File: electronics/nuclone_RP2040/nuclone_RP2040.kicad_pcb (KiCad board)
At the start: 4 copper layers, 50 x 50 mm, 42 parts, among them J1 JTAG_2X05, J2 TYPE-C-31-M-12, J3 nuclone_small_left, J4 nuclone_small_right, SW1 RESET, SW2 Bootloader, U1 MCP1702-MB, U2 TPESD0504C6

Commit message: WIP placing
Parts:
- added C10: 1u, SquantorRcl:C_0402, F.Cu at (90.3, 87.8)
- added C11: 22p, SquantorRcl:C_0402, F.Cu at (91.0, 102.4)
- added C12: 22p, SquantorRcl:C_0402, F.Cu at (93.6, 102.9)
- added C13: 1u, SquantorRcl:C_0402, F.Cu at (90.3, 91.4)
- added C15: 1u, SquantorRcl:C_0402, F.Cu at (86.4, 95.7)
- added C16: 1u, SquantorRcl:C_0402, F.Cu at (85.0, 84.6)
- added C18: 1u, SquantorRcl:C_0402, F.Cu at (87.2, 84.6)
- added C19: 1u, SquantorRcl:C_0402, F.Cu at (89.8, 86.1)
- added C20: 1u, SquantorRcl:C_0402, F.Cu at (88.3, 84.6)
- added C21: 1u, SquantorRcl:C_0402, F.Cu at (83.9, 84.6)
- added C5: 1u, SquantorRcl:C_0402, F.Cu at (79.7, 87.8)
- added C6: 1u, SquantorRcl:C_0402, F.Cu at (79.7, 91.4)
- added C7: 1u, SquantorRcl:C_0402, F.Cu at (85.3, 95.7)
- added C8: 1u, SquantorRcl:C_0402, F.Cu at (86.1, 84.6)
- added FB2: 600, SquantorRcl:L_0402, F.Cu at (90.9, 86.1)
- added R9: TBD, SquantorRcl:R_0402_hand, F.Cu at (84.2, 95.7)
- added U3: rp2040, SquantorIC:QFN56_7by7mm_RaspberryPi, F.Cu at (85.0, 90.4)
- added Y1: 12MHz, SquantorCrystal:Crystal_3225_4, F.Cu at (90.0, 98.7)
- N1: footprint Symbols:OSHW-Symbol_6.7x6mm_SilkScreen -> Symbol:OSHW-Symbol_6.7x6mm_SilkScreen
- N2: value V20220515 -> V20220527
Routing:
- net /VSS: vias 17 -> 16

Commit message: updated design rules, fixed some DRC errors
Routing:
- net /VSS: track 24.7 -> 24.3 mm, vias 16 -> 12
- net /TDO: vias 1 -> 0
- net /TDI: vias 1 -> 0

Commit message: added serial flash
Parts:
- added C22: 1u, SquantorRcl:C_0402, F.Cu at (86.7, 82.4)
- added C23: 10u, SquantorRcl:C_0603, F.Cu at (87.0, 80.1)
- added U4: MX25L3233FZBI, SquantorIC:USON-8-4x3-Macronix, F.Cu at (82.7, 81.8)
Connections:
- U3 pad 51: unconnected-(U3-Pad51) -> /microcontroller/QSPI_SD3
- U3 pad 52: unconnected-(U3-Pad52) -> /microcontroller/QSPI_SCLK
- U3 pad 53: unconnected-(U3-Pad53) -> /microcontroller/QSPI_SD0
- U3 pad 54: unconnected-(U3-Pad54) -> /microcontroller/QSPI_SD2
- U3 pad 55: unconnected-(U3-Pad55) -> /microcontroller/QSPI_SD1
- U3 pad 56: unconnected-(U3-Pad56) -> /microcontroller/QSPI_SS
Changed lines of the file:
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@@
   (net 57 "/microcontroller/AVDD")
   (net 58 "Net-(R9-Pad2)")
-  (net 59 "unconnected-(U3-Pad51)")
-  (net 60 "unconnected-(U3-Pad52)")
-  (net 61 "unconnected-(U3-Pad53)")
-  (net 62 "unconnected-(U3-Pad54)")
-  (net 63 "unconnected-(U3-Pad55)")
-  (net 64 "unconnected-(U3-Pad56)")
+  (net 59 "/microcontroller/QSPI_SD3")
+  (net 60 "/microcontroller/QSPI_SCLK")
+  (net 61 "/microcontroller/QSPI_SD0")
+  (net 62 "/microcontroller/QSPI_SD2")
+  (net 63 "/microcontroller/QSPI_SD1")
+  (net 64 "/microcontroller/QSPI_SS")
   (footprint "MountingHole:MountingHole_3.2mm_M3_Pad_Via" locked (layer "F.Cu")
     (at 63.7 64.7)
@@
   )
   (footprint "SquantorRcl:C_0402" (layer "F.Cu")
+    (at 86.7 82.4)
+    (descr "Capacitor SMD 0402, reflow soldering, AVX (see smccp.pdf)")
+    (tags "capacitor 0402")
+    (property "Sheetfile" "microcontroller.kicad_sch")
+    (property "Sheetname" "microcontroller")
+    (attr smd)
+    (fp_text reference "C22" (at 0 -1.7) (layer "F.SilkS")
+      (effects (font (size 1 1) (thickness 0.15)))
+    )
+    (fp_text value "1u" (at 0 1.7) (layer "F.Fab")
+      (effects (font (size 1 1) (thickness 0.15)))
+    )
+    (fp_line (start 0 -0.2) (end 0 0.2) (layer "F.SilkS") (width 0.15))
+    (fp_line (start 1.1 -0.55) (end 1.1 0.55) (layer "F.CrtYd") (width 0.05))
+    (fp_line (start -1.1 -0.55) (end 1.1 -0.55) (layer "F.CrtYd") (width 0.05))
+    (fp_line (start -1.1 -0.55) (end -1.1 0.55) (layer "F.CrtYd") (width 0.05))
+    (fp_line (start -1.1 0.55) (end 1.1 0.55) (layer "F.CrtYd") (width 0.05))
+    (fp_line (start 0.5 0.25) (end -0.5 0.25) (layer "F.Fab") (width 0.1))
+    (fp_line (start -0.5 0.25) (end -0.5 -0.25) (layer "F.Fab") (width 0.1))
+    (fp_line (start -0.5 -0.25) (end 0.5 -0.25) (layer "F.Fab") (width 0.1))
+    (fp_line (start 0.5 -0.25) (end 0.5 0.25) (layer "F.Fab") (width 0.1))
+    (pad "1" smd rect (at -0.55 0) (size 0.6 0.6) (layers "F.Cu" "F.Paste" "F.Mask")
+      (net 5 "/VSS") (pintype "passive"))
+    (pad "2" smd rect (at 0.55 0) (size 0.6 0.6) (layers "F.Cu" "F.Paste" "F.Mask")
+      (net 3 "/VDD") (pintype "passive"))
+    (model "${KICAD6_3DMODEL_DIR}//Capacitor_SMD.3dshapes/C_0402_1005Metric.step"
+      (offset (xyz 0 0 0))
+      (scale (xyz 1 1 1))
+      (rotate (xyz 0 0 0))
+    )
+  )
+  (footprint "SquantorRcl:C_0402" (layer "F.Cu")
     (at 86.4 95.7 90)
     (descr "Capacitor SMD 0402, reflow soldering, AVX (see smccp.pdf)")
@@
       (net 56 "/microcontroller/1.1V") (pinfunction "DVDD") (pintype "power_in"))
     (pad "51" smd rect (at -0.6 -3.4375 270) (size 0.875 0.2) (layers "F.Cu" "F.Paste" "F.Mask")
-      (net 59 "unconnected-(U3-Pad51)") (pinfunction "QSPI_SD3") (pintype "bidirectional"))
+      (net 59 "/microcontroller/QSPI_SD3") (pinfunction "QSPI_SD3") (pintype "bidirectional"))
     (pad "52" smd rect (at -1 -3.4375 270) (size 0.875 0.2) (layers "F.Cu" "F.Paste" "F.Mask")
-      (net 60 "unconnected-(U3-Pad52)") (pinfunction "QSPI_SCLK") (pintype "output"))
+      (net 60 "/microcontroller/QSPI_SCLK") (pinfunction "QSPI_SCLK") (pintype "output"))
     (pad "53" smd rect (at -1.4 -3.4375 270) (size 0.875 0.2) (layers "F.Cu" "F.Paste" "F.Mask")
-      (net 61 "unconnected-(U3-Pad53)") (pinfunction "QSPI_SD0") (pintype "bidirectional"))
+      (net 61 "/microcontroller/QSPI_SD0") (pinfunction "QSPI_SD0") (pintype "bidirectional"))
     (pad "54" smd rect (at -1.8 -3.4375 270) (size 0.875 0.2) (layers "F.Cu" "F.Paste" "F.Mask")
-      (net 62 "unconnected-(U3-Pad54)") (pinfunction "QSPI_SD2") (pintype "bidirectional"))
+      (net 62 "/microcontroller/QSPI_SD2") (pinfunction "QSPI_SD2") (pintype "bidirectional"))
     (pad "55" smd rect (at -2.2 -3.4375 270) (size 0.875 0.2) (layers "F.Cu" "F.Paste" "F.Mask")
-      (net 63 "unconnected-(U3-Pad55)") (pinfunction "QSPI_SD1") (pintype "bidirectional"))
+      (net 63 "/microcontroller/QSPI_SD1") (pinfunction "QSPI_SD1") (pintype "bidirectional"))
     (pad "56" smd rect (at -2.6 -3.4375 270) (size 0.875 0.2) (layers "F.Cu" "F.Paste" "F.Mask")
-      (net 64 "unconnected-(U3-Pad56)") (pinfunction "QSPI_SS_N") (pintype "output"))
+      (net 64 "/microcontroller/QSPI_SS") (pinfunction "QSPI_SS_N") (pintype "output"))
     (pad "57" smd rect (at 0 0) (size 3.2 3.2) (layers "F.Cu")
       (net 5 "/VSS") (pinfunction "GND") (pintype "power_in"))
@@
       (rotate (xyz 0 0 0))
     )
+  )
+  (footprint "SquantorRcl:C_0603" (layer "F.Cu")
+    (at 87 80.1)
+    (descr "Capacitor SMD 0603, reflow soldering, AVX (see smccp.pdf)")
+    (tags "capacitor 0603")
+    (property "Sheetfile" "microcontroller.kicad_sch")
+    (property "Sheetname" "microcontroller")
+    (attr smd)
+    (fp_text reference "C23" (at 0 -1.9) (layer "F.SilkS")
+      (effects (font (size 1 1) (thickness 0.15)))
+    )
+    (fp_text value "10u" (at 0 1.9) (layer "F.Fab")
+      (effects (font (size 1 1) (thickness 0.15)))
+    )
+    (fp_line (start 0 -0.35) (end 0 0.35) (layer "F.SilkS") (width 0.15))
+    (fp_line (start -1.4 0.7) (end 1.4 0.7) (layer "F.CrtYd") (width 0.05))
+    (fp_line (start 1.4 -0.7) (end 1.4 0.7) (layer "F.CrtYd") (width 0.05))
+    (fp_line (start -1.4 -0.7) (end -1.4 0.7) (layer "F.CrtYd") (width 0.05))
+    (fp_line (start -1.4 -0.7) (end 1.4 -0.7) (layer "F.CrtYd") (width 0.05))
+    (fp_line (start -0.8 -0.4) (end 0.8 -0.4) (layer "F.Fab") (width 0.1))
+    (fp_line (start 0.8 -0.4) (end 0.8 0.4) (layer "F.Fab") (width 0.1))
+    (fp_line (start -0.8 0.4) (end -0.8 -0.4) (layer "F.Fab") (width 0.1))
+    (fp_line (start 0.8 0.4) (end -0.8 0.4) (layer "F.Fab") (width 0.1))
+    (pad "1" smd rect (at -0.75 0) (size 0.8 0.9) (layers "F.Cu" "F.Paste" "F.Mask")
+      (net 5 "/VSS") (pintype "passive"))
+    (pad "2" smd rect (at 0.75 0) (size 0.8 0.9) (layers "F.Cu" "F.Paste" "F.Mask")
+      (net 3 "/VDD") (pintype "passive"))
+    (model "${KICAD6_3DMODEL_DIR}/Capacitor_SMD.3dshapes/C_0603_1608Metric.step"
+      (offset (xyz 0 0 0))
+      (scale (xyz 1 1 1))
+      (rotate (xyz 0 0 0))
+    )
+  )
+  (footprint "SquantorIC:USON-8-4x3-Macronix" (layer "F.Cu")
+    (at 82.665 81.835)
+    (descr "USON 8 pin 4 by 3mm size as specified by Macronix")
+    (tags "USON-8 4x3mm Macronix")
+    (property "Sheetfile" "microcontroller.kicad_sch")
+    (property "Sheetname" "microcontroller")
+    (attr smd)
+    (fp_text reference "U4" (at 0 -2.9) (layer "F.SilkS")
+      (effects (font (size 1 1) (thickness 0.15)))
+    )
+    (fp_text value "MX25L3233FZBI" (at 0 2.8) (layer "F.Fab")
+      (effects (font (size 1 1) (thickness 0.15)))
+    )
+    (fp_line (start -1.5 2) (end 1.5 2) (layer "F.SilkS") (width 0.12))
+    (fp_line (start 1.5 -2) (end -1.5 -2) (layer "F.SilkS") (width 0.12))
+    (fp_circle (center -1.7 -2.2) (end -1.5 -2.2) (layer "F.SilkS") (width 0.12) (fill none))
+    (fp_line (start -1.9 -2.3) (end -1.9 2.4) (layer "F.CrtYd") (width 0.025))
+    (fp_line (start 1.9 -2.3) (end -1.9 -2.3) (layer "F.CrtYd") (width 0.025))
+    (fp_line (start -1.9 2.4) (end 1.9 2.4) (layer "F.CrtYd") (width 0.025))
+    (fp_line (start 1.9 2.4) (end 1.9 -2.3) (layer "F.CrtYd") (width 0.025))
+    (fp_line (start -1.5 -2) (end -1.5 2) (layer "F.Fab") (width 0.1))
+    (fp_line (start 1.5 2) (end 1.5 -2) (layer "F.Fab") (width 0.1))
+    (pad "1" smd rect locked (at -1.2 -1.2) (size 0.8 0.4) (layers "F.Cu" "F.Paste" "F.Mask")
+      (net 64 "/microcontroller/QSPI_SS") (pinfunction "CS/") (pintype "input"))
+    (pad "2" smd rect locked (at -1.2 -0.4) (size 0.8 0.4) (layers "F.Cu" "F.Paste" "F.Mask")
+      (net 63 "/microcontroller/QSPI_SD1") (pinfunction "SO_SIO1") (pintype "bidirectional"))
+    (pad "3" smd rect locked (at -1.2 0.4) (size 0.8 0.4) (layers "F.Cu" "F.Paste" "F.Mask")
+      (net 62 "/microcontroller/QSPI_SD2") (pinfunction "WP/_SIO2") (pintype "bidirectional"))
+    (pad "4" smd rect locked (at -1.2 1.2) (size 0.8 0.4) (layers "F.Cu" "F.Paste" "F.Mask")
+      (net 5 "/VSS") (pinfunction "GND") (pintype "power_in"))
+    (pad "5" smd rect locked (at 1.2 1.2) (size 0.8 0.4) (layers "F.Cu" "F.Paste" "F.Mask")
+      (net 61 "/microcontroller/QSPI_SD0") (pinfunction "SI_SIO0") (pintype "power_in"))
+    (pad "6" smd rect locked (at 1.2 0.4) (size 0.8 0.4) (layers "F.Cu" "F.Paste" "F.Mask")
+      (net 60 "/microcontroller/QSPI_SCLK") (pinfunction "SCLK") (pintype "input"))
+    (pad "7" smd rect locked (at 1.2 -0.4) (size 0.8 0.4) (layers "F.Cu" "F.Paste" "F.Mask")
+      (net 59 "/microcontroller/QSPI_SD3") (pinfunction "HOLD/_SIO3") (pintype "bidirectional"))
+    (pad "8" smd rect locked (at 1.2 -1.2) (size 0.8 0.4) (layers "F.Cu" "F.Paste" "F.Mask")
+      (net 3 "/VDD") (pinfunction "VCC") (pintype "power_in"))
+    (pad "9" smd rect locked (at 0 -0.8) (size 0.2 0.8) (layers "F.Cu" "F.Paste" "F.Mask")
+      (net 5 "/VSS") (pinfunction "GND") (pintype "power_in"))
+    (pad "9" smd rect locked (at 0 0.8) (size 0.2 0.8) (layers "F.Cu" "F.Paste" "F.Mask")
+      (net 5 "/VSS") (pinfunction "GND") (pintype "power_in"))
+    (model "${KISYS3DMOD}/Package_SON.3dshapes/WSON-8_4x4mm_P0.8mm.step"
+      (offset (xyz 0 0 0))
+      (scale (xyz 0.7 1 1))
+      (rotate (xyz 0 0 0))
+    )

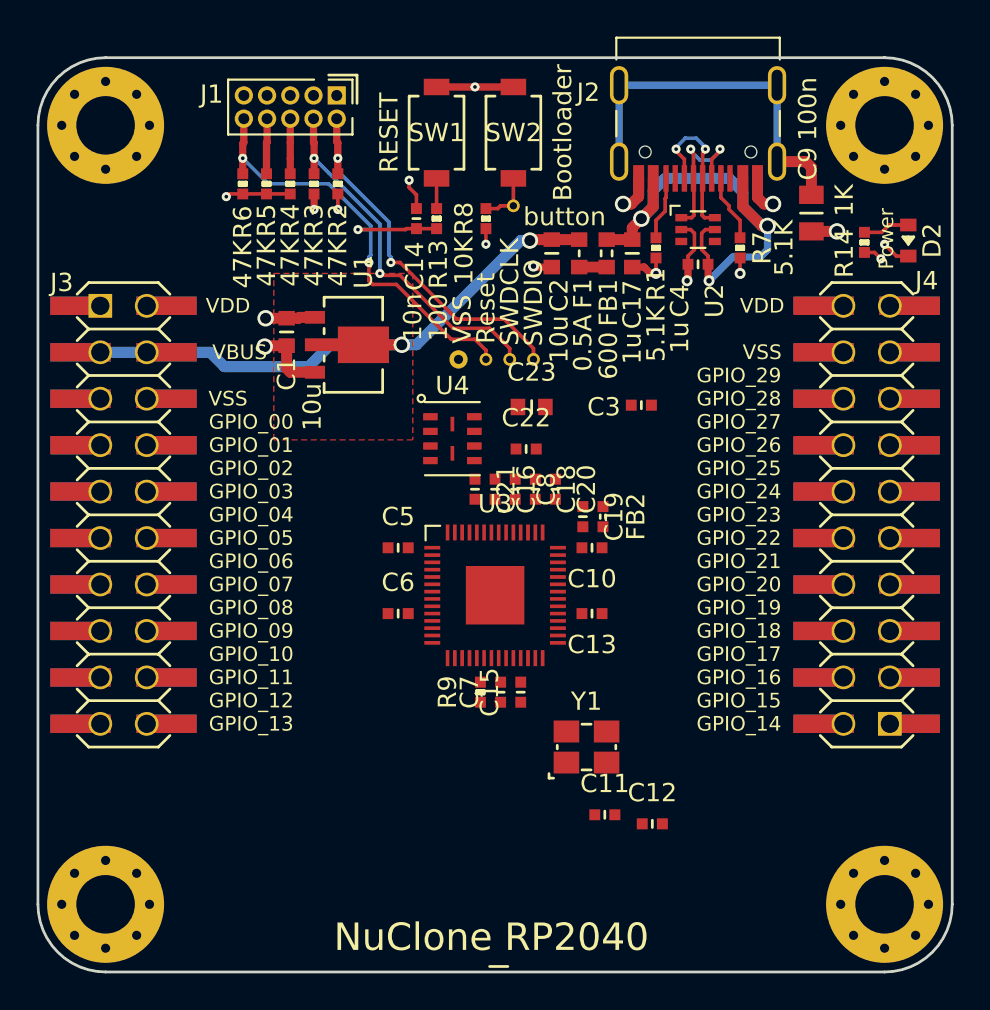
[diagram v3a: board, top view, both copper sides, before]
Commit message: further placing and routing
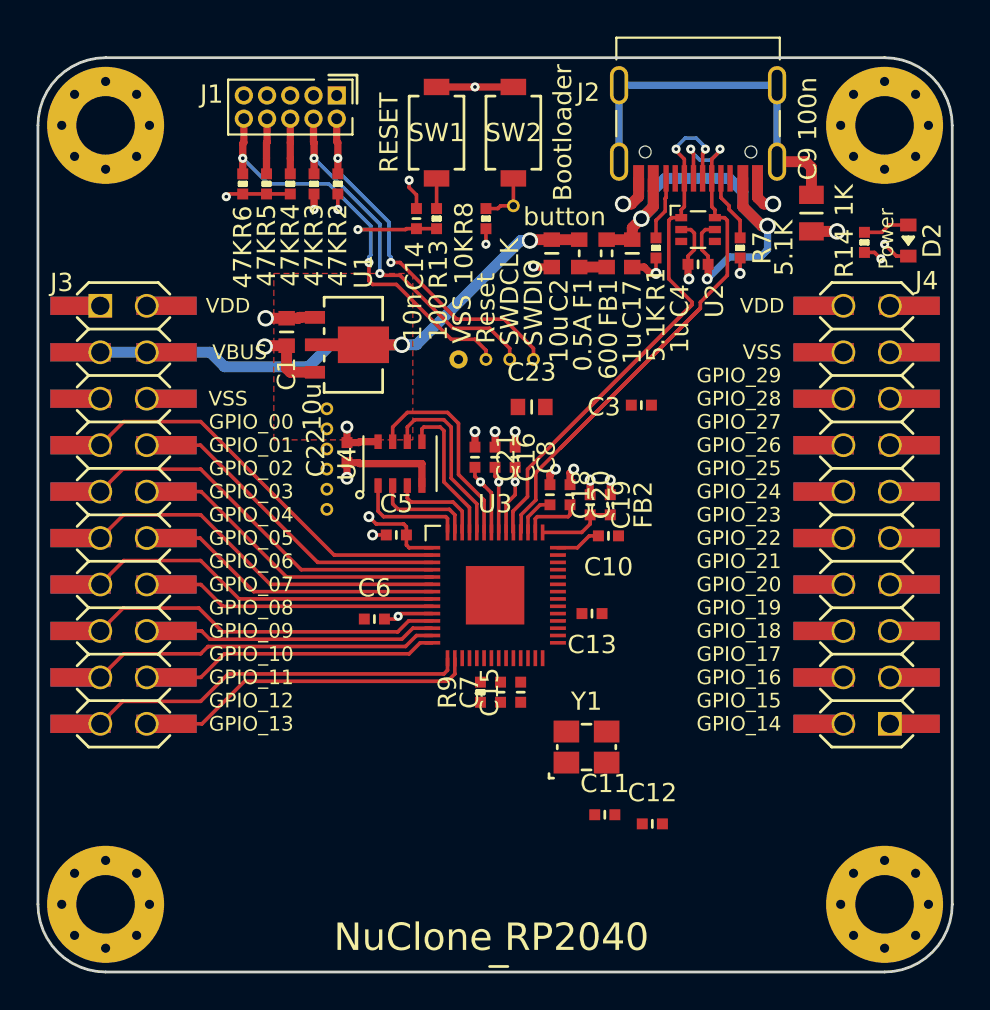
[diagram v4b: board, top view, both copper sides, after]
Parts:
- added TP10: QSPI_SD2, SquantorTestPoints:TestPoint_hole_H04R07, B.Cu at (75.8, 83.5)
- added TP11: QSPI_SD3, SquantorTestPoints:TestPoint_hole_H04R07, B.Cu at (75.8, 80.2)
- added TP6: QSPI_SS, SquantorTestPoints:TestPoint_hole_H04R07, B.Cu at (75.8, 85.7)
- added TP7: QSPI_SCLK, SquantorTestPoints:TestPoint_hole_H04R07, B.Cu at (75.8, 81.3)
- added TP8: QSPI_SD0, SquantorTestPoints:TestPoint_hole_H04R07, B.Cu at (75.8, 82.4)
- added TP9: QSPI_SD1, SquantorTestPoints:TestPoint_hole_H04R07, B.Cu at (75.8, 84.6)
- moved C22 9.80 mm to (76.9, 82.6), turned to 90 degrees
- moved U4 3.17 mm to (79.8, 83.2), turned to 90 degrees
- moved C16 1.75 mm to (85.0, 82.8)
- moved C21 1.75 mm to (83.9, 82.8)
- moved C8 1.75 mm to (86.1, 82.8)
- moved C6 1.33 mm to (78.4, 91.7)
- moved C10 1.11 mm to (91.2, 87.2)
- moved C18 0.85 mm to (88.0, 84.9)
- moved C20 0.85 mm to (89.1, 84.9)
- moved C19 0.76 mm to (90.2, 85.5)
- moved FB2 0.76 mm to (91.3, 85.5)
- moved C5 0.71 mm to (79.6, 87.1)
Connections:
- U2 pad 1: /DN -> /DP
- U2 pad 6: /DP -> /DN
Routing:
- net /DN: track 8.44 -> 41.2 mm
- net /DP: track 9.14 -> 40.9 mm
- net /VDD: track 10.4 -> 34.5 mm, vias 5 -> 11
- net /GPIO_00: track 0.00 -> 21.7 mm
- net /GPIO_02: track 0.00 -> 20.9 mm
- net /GPIO_12: track 0.00 -> 20.9 mm
- net /GPIO_04: track 0.00 -> 20.3 mm
- net /GPIO_06: track 0.00 -> 19.6 mm
- net /GPIO_08: track 0.00 -> 19.5 mm
- net /GPIO_10: track 0.00 -> 19.1 mm
- net /GPIO_13: track 0.00 -> 17.8 mm
- net /GPIO_01: track 0.00 -> 17.2 mm
- net /GPIO_03: track 0.00 -> 16.5 mm
- net /GPIO_05: track 0.00 -> 15.7 mm
- net /GPIO_11: track 0.00 -> 15.3 mm
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
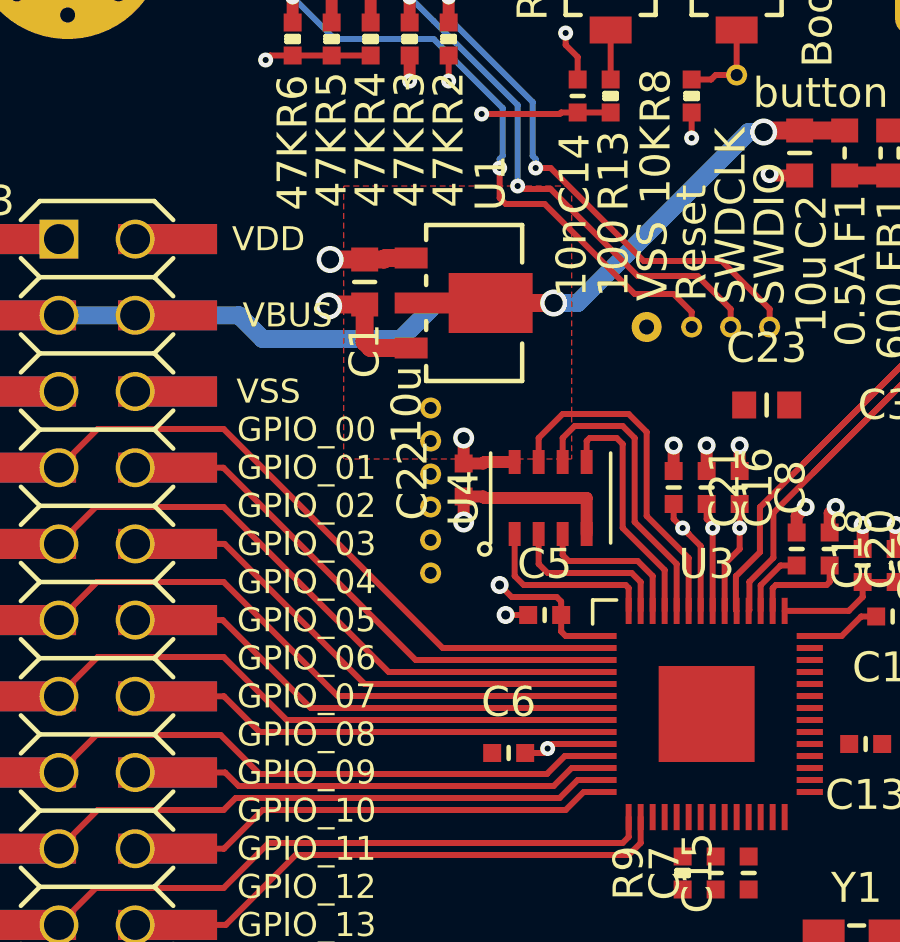
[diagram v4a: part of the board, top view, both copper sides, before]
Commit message: further routing, added a QSPI debug connector for easy probing with logic analyser
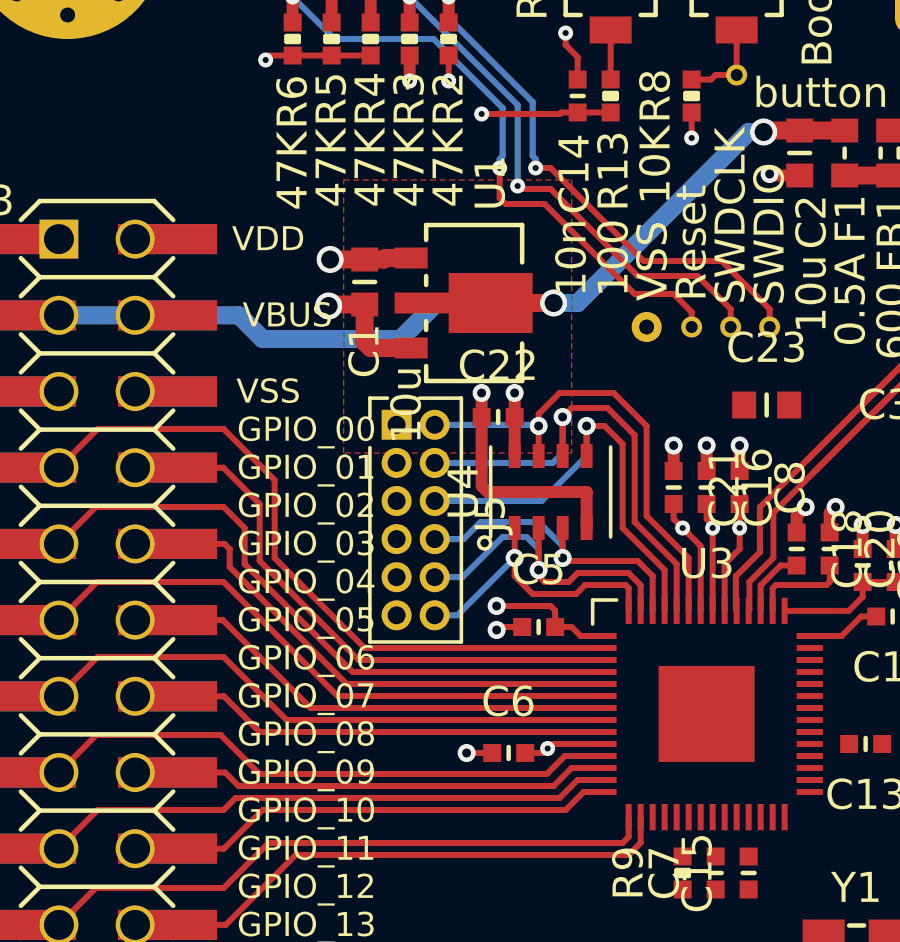
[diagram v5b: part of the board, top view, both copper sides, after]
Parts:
- removed TP10: QSPI_SD2, SquantorTestPoints:TestPoint_hole_H04R07
- removed TP11: QSPI_SD3, SquantorTestPoints:TestPoint_hole_H04R07
- removed TP6: QSPI_SS, SquantorTestPoints:TestPoint_hole_H04R07
- removed TP7: QSPI_SCLK, SquantorTestPoints:TestPoint_hole_H04R07
- removed TP8: QSPI_SD0, SquantorTestPoints:TestPoint_hole_H04R07
- removed TP9: QSPI_SD1, SquantorTestPoints:TestPoint_hole_H04R07
- added J5: Conn_02x06_Odd_Even, SquantorConnectors:Header-0127-2X06-H006, F.Cu at (75.3, 83.9)
- moved C22 2.39 mm to (78.0, 80.5), turned to 0 degrees
- moved C5 0.45 mm to (79.4, 87.5)
- moved U4 0.20 mm to (79.8, 83.0)
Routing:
- net /microcontroller/QSPI_SD0: track 8.17 -> 15.3 mm, vias 0 -> 1
- net /microcontroller/QSPI_SCLK: track 9.87 -> 16.2 mm, vias 0 -> 1
- net /microcontroller/QSPI_SD1: track 5.21 -> 10.7 mm, vias 0 -> 1
- net /microcontroller/QSPI_SD2: track 5.15 -> 10.6 mm, vias 0 -> 1
- net /microcontroller/QSPI_SD3: track 11.5 -> 16.0 mm, vias 0 -> 1
- net /microcontroller/QSPI_SS: track 5.73 -> 9.63 mm, vias 0 -> 1
- net /VSS: track 36.3 -> 39.0 mm, vias 20 -> 21
- net /GPIO_00: track 21.7 -> 23.2 mm
- net /GPIO_01: track 17.2 -> 18.3 mm
- net /VDD: track 34.5 -> 33.5 mm
- net /GPIO_02: track 20.9 -> 21.6 mm
